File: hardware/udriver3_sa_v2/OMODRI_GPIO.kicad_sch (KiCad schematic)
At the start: 1 part, among them U1 TMS320F28388D

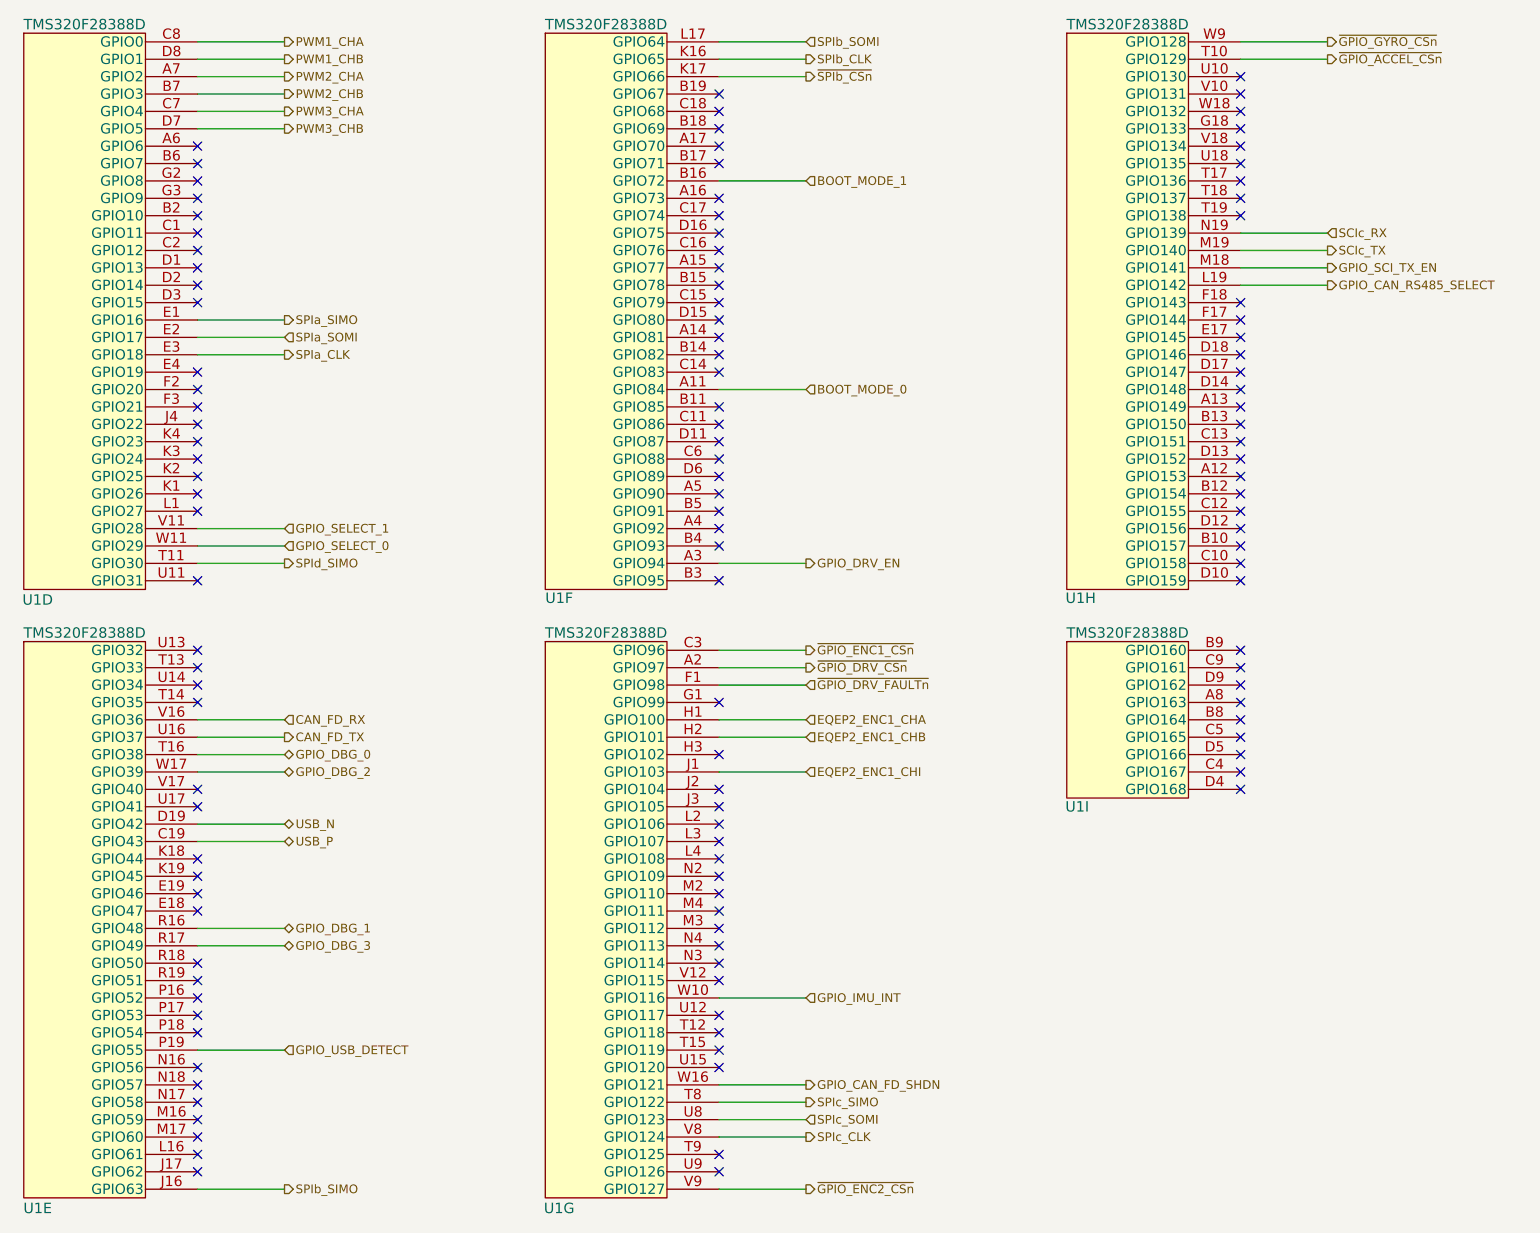
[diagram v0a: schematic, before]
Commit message: Udriver3 Single Axis V2. Update on RS485 communication (add McBSP + CLB).
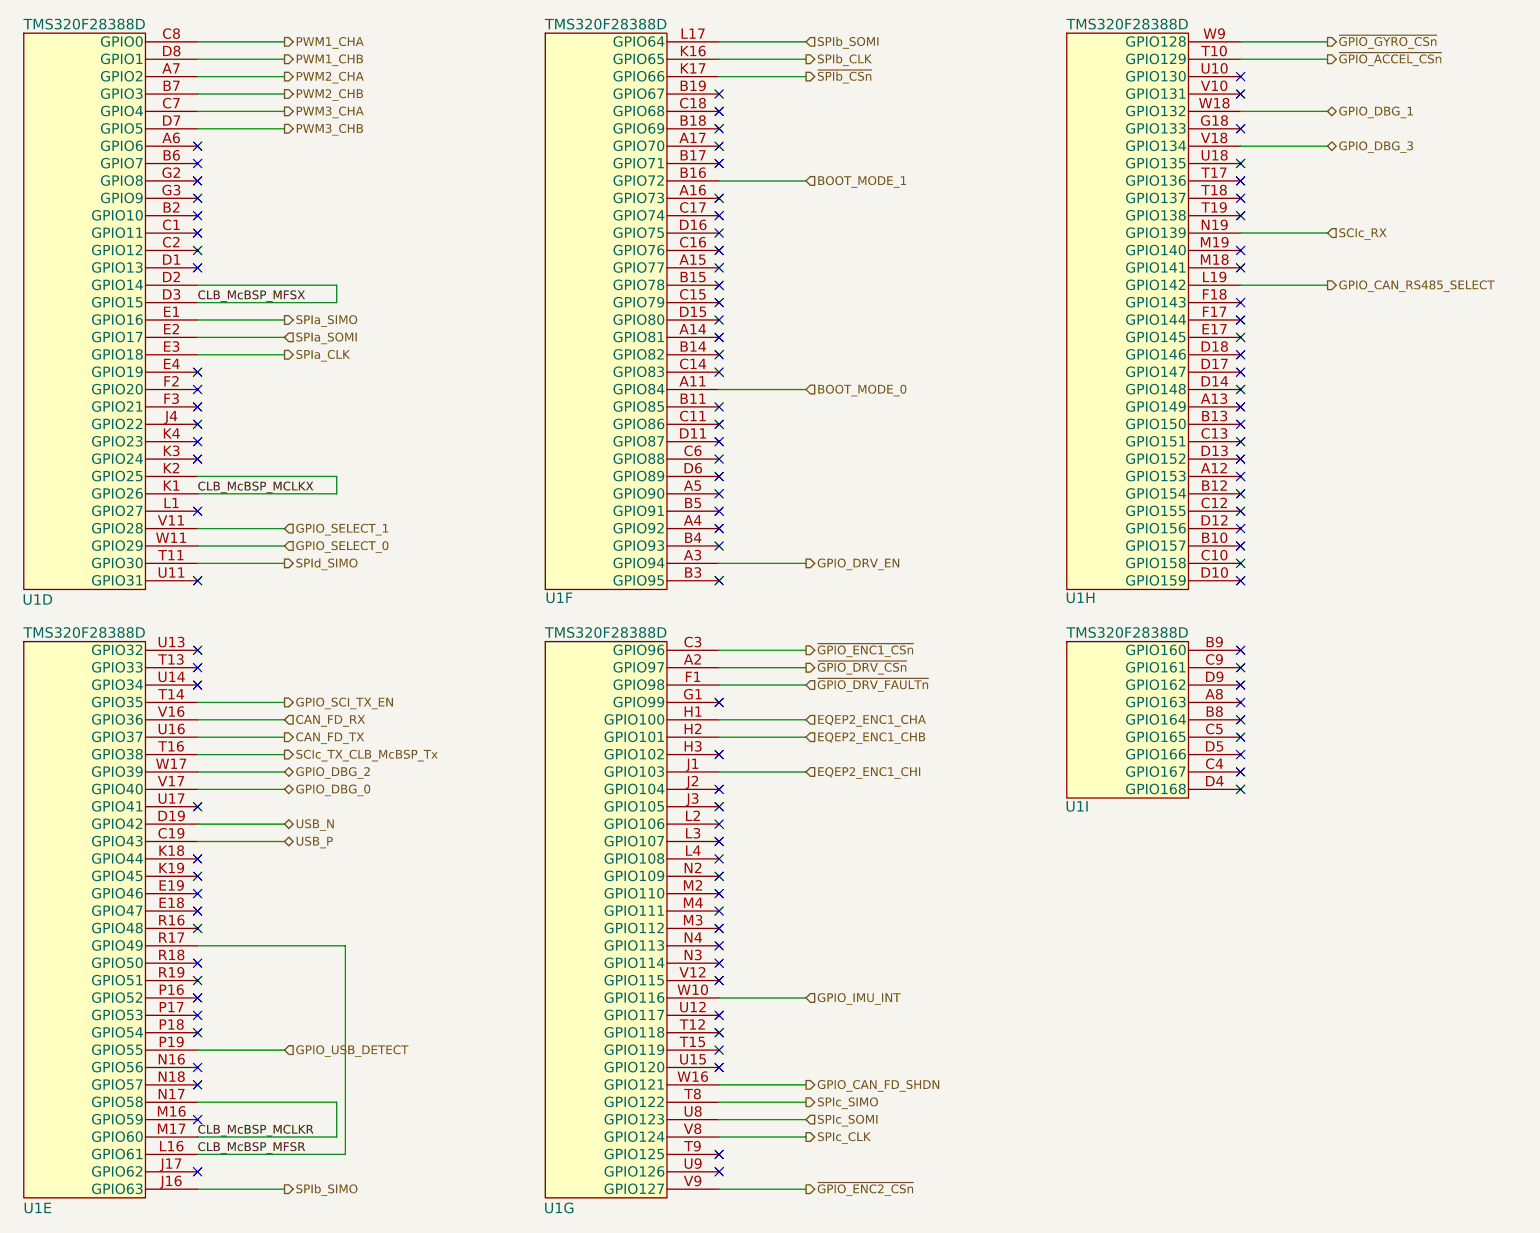
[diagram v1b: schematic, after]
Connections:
- net GPIO_DBG_0: now also U1.V17 (GPIO40); no longer U1.T16 (GPIO38)
- net GPIO_DBG_1: now also U1.W18 (GPIO132); no longer U1.R16 (GPIO48)
- net GPIO_DBG_3: now also U1.V18 (GPIO134); no longer U1.R17 (GPIO49)
- net GPIO_SCI_TX_EN: now also U1.T14 (GPIO35); no longer U1.M18 (GPIO141)
- net CLB_McBSP_MFSX: now reaches U1.D2 (GPIO14)
- net CLB_McBSP_MFSX: now also U1.D3 (GPIO15)
- net CLB_McBSP_MCLKX: now reaches U1.K1 (GPIO26)
- net CLB_McBSP_MCLKX: now also U1.K2 (GPIO25)
- net CLB_McBSP_MFSR: now reaches U1.L16 (GPIO61)
- net CLB_McBSP_MFSR: now also U1.R17 (GPIO49)
- net CLB_McBSP_MCLKR: now reaches U1.M17 (GPIO60)
- net CLB_McBSP_MCLKR: now also U1.N17 (GPIO58)
- net SCIc_TX: no longer names the net of U1.M19 (GPIO140)
- new net SCIc_TX_CLB_McBSP_Tx: U1.T16 (GPIO38)
- no-connect marks 123 -> 115
